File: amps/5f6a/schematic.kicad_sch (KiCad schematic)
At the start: 60 parts, among them T3 2R sec

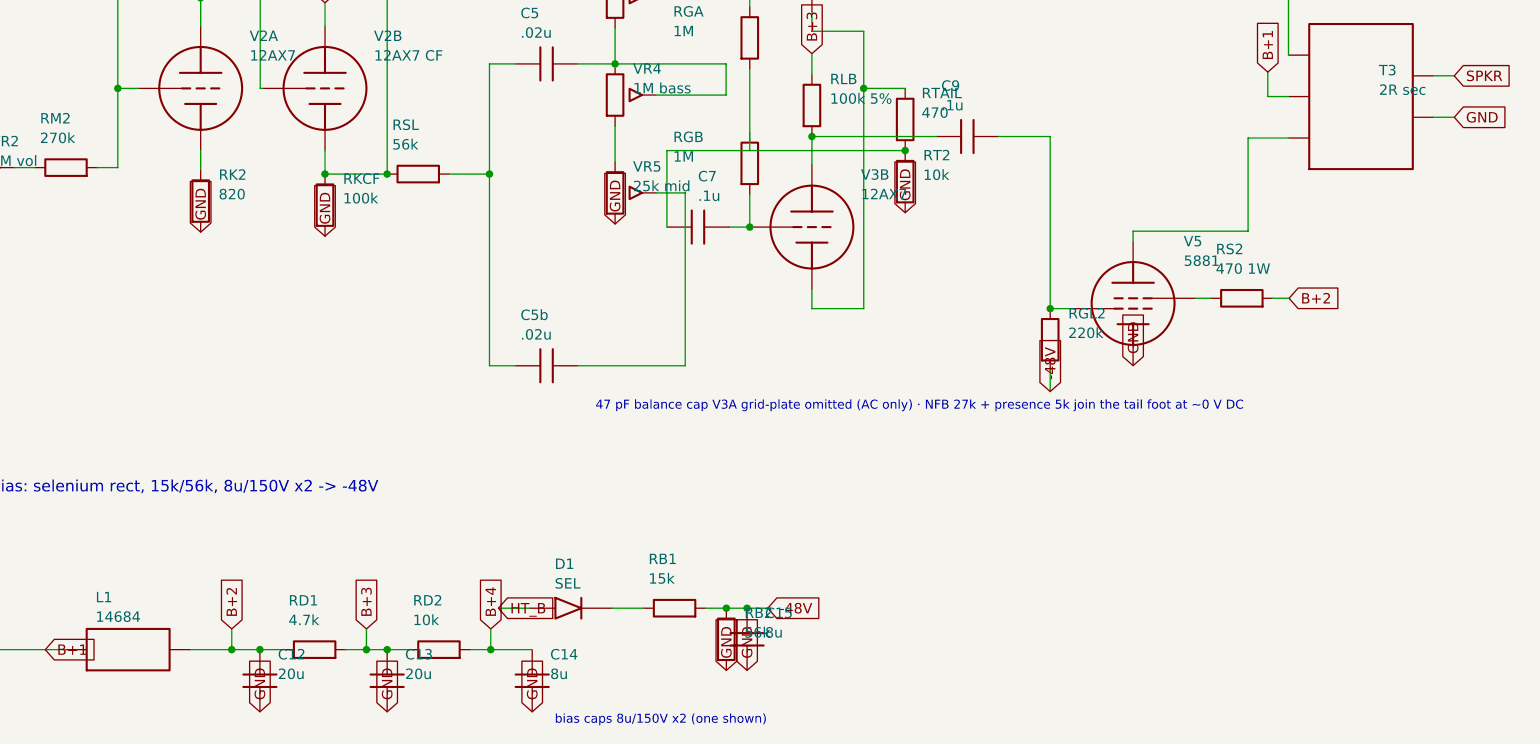
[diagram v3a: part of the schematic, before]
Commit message: Fix: eleven per-amp claims that had drifted from the circuits they describe
Prose that contradicted the corpus it sits in:

* The 5F4 called its ancestor "the 5E-series Super not yet published in this
  archive" while its own meta.yaml derives it from 5E4-A and that circuit has a
  page; the 5F1 said its lineage edge "lands when amps/5e1 exists" while the
  sidebar already links the 5E1. Both now name the documented ancestor. The
  whole corpus was swept for the pattern: 5F2-A's 5F2, 5E5-A's 5E5, 5D3's 5C3,
  5F2-A's and 5F10's earlier revisions and DR103's Sound City are all still
  genuinely absent, so those stay.
* The 5E6-A said its front end gates "within the usual tolerance (worst node
  29.8%)" against a +/-20% convention — a sentence that contradicts itself and
  understates the miss besides. It now states the four nodes that miss, the
  numbers they miss by, and the one dropper-current fault behind all four,
  which is what its own meta.yaml already said. Same defect class as the 5E4-A
  fix in 4c65fa8.
* The 5E5-A's parts list opened "No schematic.kicad_sch is authored in this
  delivery" — one has been authored. Deleted.
* Repo paths were rendering on public pages: four SOURCES entries (5F1, 5E3,
  5F2-A, 5F6, 5F6-A) named amps/<id>/layout.svg, and the 5E5-A, 5E6-A and 5F10
  pages cited voltages.yaml, netlist.cir, verify_amps.py and CONTRIBUTING.md in
  running prose. All reworded as visitor documentation. The 5F10's layout also
  described its own schematic page as "reproduced", which is the one word this
  project must never use about a factory drawing.

Circuit elements that existed only as a caption:

* The 5F6-A's headline change from the 5F6 is the presence control, and it was
  a line of schematic text. It is drawn now — 27k feedback resistor, 5k pot and
  its 0.1 uF wiper cap, at the phase-inverter tail — with designators, parts-list
  rows and chassis-edge placement on both board styles.
* The 5F4's 56k feedback and 5k presence were the same, an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
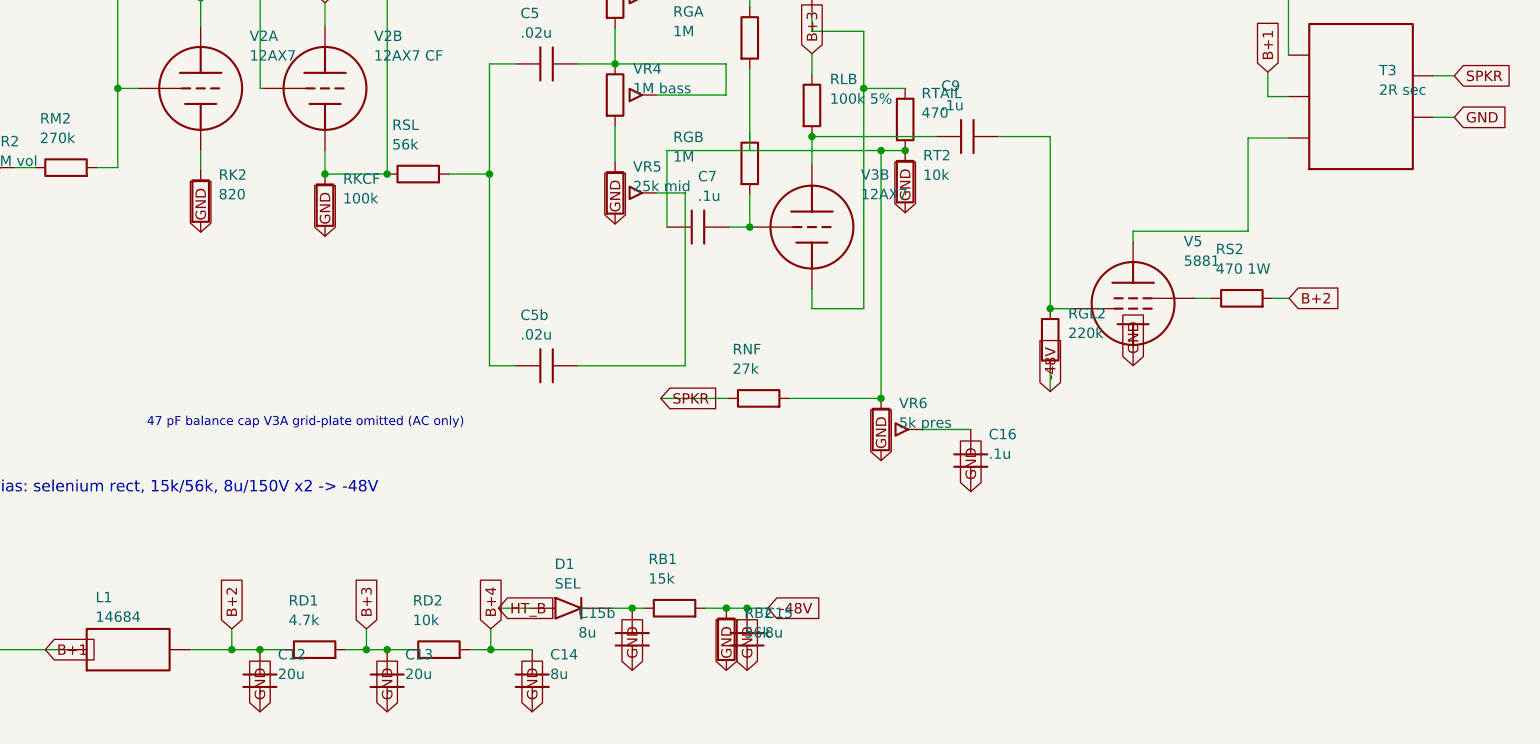
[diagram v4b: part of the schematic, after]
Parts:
- added C15b: 8u, symbol cx:C
- added C16: .1u, symbol cx:C
- added RNF: 27k, symbol cx:R
- added VR6: 5k pres, symbol cx:POT
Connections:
- net GND: now also C15b.2, C16.2, VR6.3
- net SPKR: now also RNF.1
- net at D1.2 (K), RB1.1: now also C15b.1
- net at C7.1, RGA.2, RT2.1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: now also RNF.2, VR6.1
- new net: C16.1, VR6.2 (W)
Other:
- note added: "47 pF balance cap V3A grid-plate omitted (AC only)"
- note removed: "47 pF balance cap V3A grid-plate omitted (AC only) · NFB 27k + presence 5k join the tail foot at ~0 V DC"
- note removed: "bias caps 8u/150V x2 (one shown)"
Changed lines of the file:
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@@
   (wire (pts (xy 158.75 116.62) (xy 168.91 116.62))
     (stroke (width 0) (type default)))
-  (text "47 pF balance cap V3A grid-plate omitted (AC only) · NFB 27k + presence 5k join the tail foot at ~0 V DC" (at 150 148 0)
+  (text "47 pF balance cap V3A grid-plate omitted (AC only)" (at 95 150 0)
     (effects (font (size 1.1 1.1)) (justify left)))
+  (junction (at 185 116.62) (diameter 0) (color 0 0 0 0))
+  (wire (pts (xy 185 116.62) (xy 185 147))
+    (stroke (width 0) (type default)))
+  (junction (at 185 147) (diameter 0) (color 0 0 0 0))
+  (symbol (lib_id "cx:R") (at 170 147 90) (unit 1)
+    (in_bom yes) (on_board yes)
+    (property "Reference" "RNF" (at 166.8 141 270) (effects (font (size 1.27 1.27)) (justify left)))
+    (property "Value" "27k" (at 166.8 143.4 270) (effects (font (size 1.27 1.27)) (justify left))))
+  (wire (pts (xy 173.81 147) (xy 185 147))
+    (stroke (width 0) (type default)))
+  (wire (pts (xy 158 147) (xy 166.19 147))
+    (stroke (width 0) (type default)))
+  (global_label "SPKR" (shape input) (at 158 147 180)
+    (effects (font (size 1.27 1.27)) (justify left)))
+  (symbol (lib_id "cx:POT") (at 185 150.81 0) (unit 1)
+    (in_bom yes) (on_board yes)
+    (property "Reference" "VR6" (at 187.2 147.61 0) (effects (font (size 1.27 1.27)) (justify left)))
+    (property "Value" "5k pres" (at 187.2 150.01 0) (effects (font (size 1.27 1.27)) (justify left))))
+  (global_label "GND" (shape input) (at 185 154.62 270)
+    (effects (font (size 1.27 1.27)) (justify left)))
+  (wire (pts (xy 190.08 150.81) (xy 196 150.81))
+    (stroke (width 0) (type default)))
+  (symbol (lib_id "cx:C") (at 196 154.62 0) (unit 1)
+    (in_bom yes) (on_board yes)
+    (property "Reference" "C16" (at 198.2 151.42 0) (effects (font (size 1.27 1.27)) (justify left)))
+    (property "Value" ".1u" (at 198.2 153.82 0) (effects (font (size 1.27 1.27)) (justify left))))
+  (global_label "GND" (shape input) (at 196 158.43 270)
+    (effects (font (size 1.27 1.27)) (justify left)))
   (wire (pts (xy 176.53 80.9) (xy 194.31 80.9))
     (stroke (width 0) (type default)))
@@
   (wire (pts (xy 152.07 172.72) (xy 155.88 172.72))
     (stroke (width 0) (type default)))
+  (junction (at 154.5 172.72) (diameter 0) (color 0 0 0 0))
+  (symbol (lib_id "cx:C") (at 154.5 176.53 0) (unit 1)
+    (in_bom yes) (on_board yes)
+    (property "Reference" "C15b" (at 147.9 173.33 0) (effects (font (size 1.27 1.27)) (justify left)))
+    (property "Value" "8u" (at 147.9 175.73 0) (effects (font (size 1.27 1.27)) (justify left))))
+  (global_label "GND" (shape input) (at 154.5 180.34 270)
+    (effects (font (size 1.27 1.27)) (justify left)))
   (symbol (lib_id "cx:R") (at 159.69 172.72 90) (unit 1)
     (in_bom yes) (on_board yes)
@@
   (global_label "-48V" (shape input) (at 171.12 172.72 0)
     (effects (font (size 1.27 1.27)) (justify left)))
-  (text "bias caps 8u/150V x2 (one shown)" (at 145 186.5 0)
-    (effects (font (size 1.1 1.1)) (justify left)))
   (sheet_instances (path "/" (page "1")))
 )

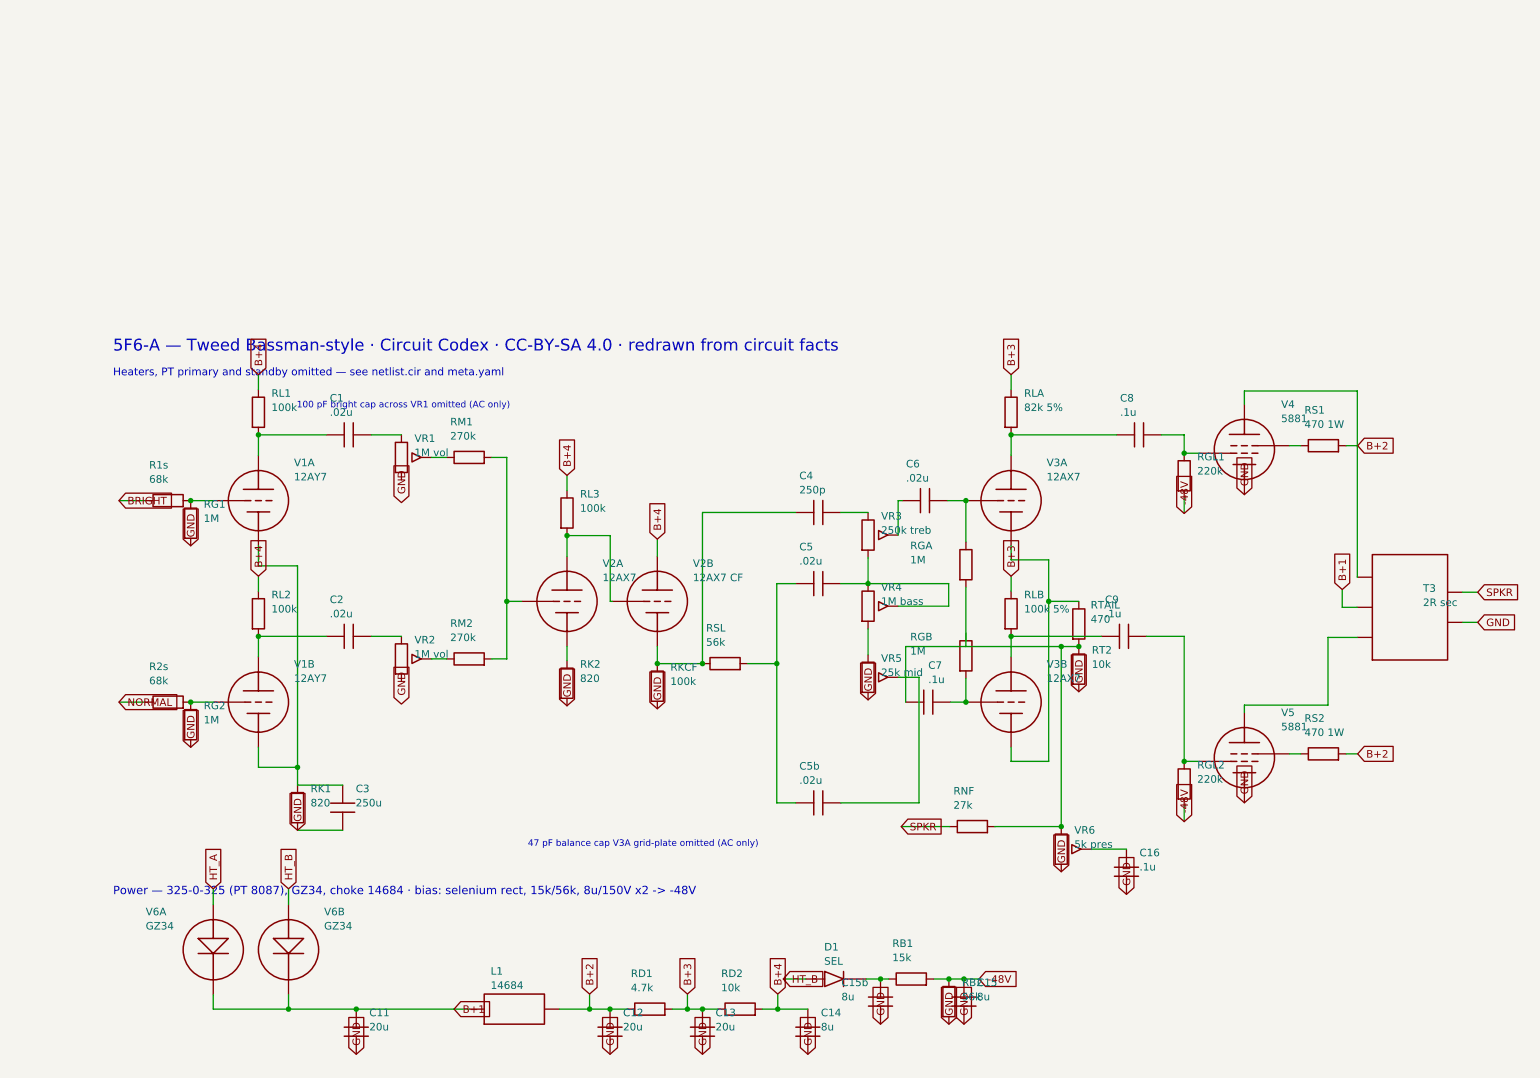
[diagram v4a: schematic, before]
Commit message: Update: regenerate every drawing the four merged units changed
The four parallel units all rewrote generators, so their committed artifacts
were each generated against only their own third of the merged pipeline. Every
schematic, both layout styles, the social cards and the manifest are rebuilt
here from the merged sources, so what ships is what the merged generators draw.

One integration fault the rebuild exposed, invisible to any single unit:

- 5E5-A: the note explaining that the Presence wiper and the 100k feedback
  resistor land on V3A's GRID (not its cathode, as on the 5F4) was added as a
  hand-placed `s.text()` at a coordinate chosen before the sheet gained a
  reserved notes band. Merged, it printed through the -32V bias label. Moved to
  `note()`, which wraps prose into that band — the exact failure mode the band
  was built to end.

Three conflicts resolved against docs/lettering-conventions.md rather than by
picking a side, since two units had corrected the same lines for different
reasons:

- 5E5-A tone/feedback caps take the corrected designators (C7, C8, C9, RNF —
  `C_tr1`/`C_NFB` were generator identifiers that had leaked onto a published
  board) with the house-derived lettering (`.01u 400V`, `500p`, `.1u 200V`).
  Dropping the working voltage or writing `.0005u` would have lost a rating the
  source prints and re-broken the pF/µF decade rule.
- 5D3 C6 and 6G6-B's three cathode resistors take the SI-prefix form the
  convention binds (`.005u`, `2.7k`, `1.5k`), keeping the ground-flag direction
  fix and the removal of the second `gnd()` that shorted each cathode it biased.
- 5F6-A's bias supply keeps both 8 µF cans drawn — the second was previously a
  parenthetical claiming one of two was shown — at the coordinates that clear
  the title-block strip.

All gates green, including check_value_consistency at zero disagreements.

🤖 Generated with [Claude Code](https://claude.com/claude-code)

Co-Authored-By: Claude Fable 5 <noreply@anthropic.com>
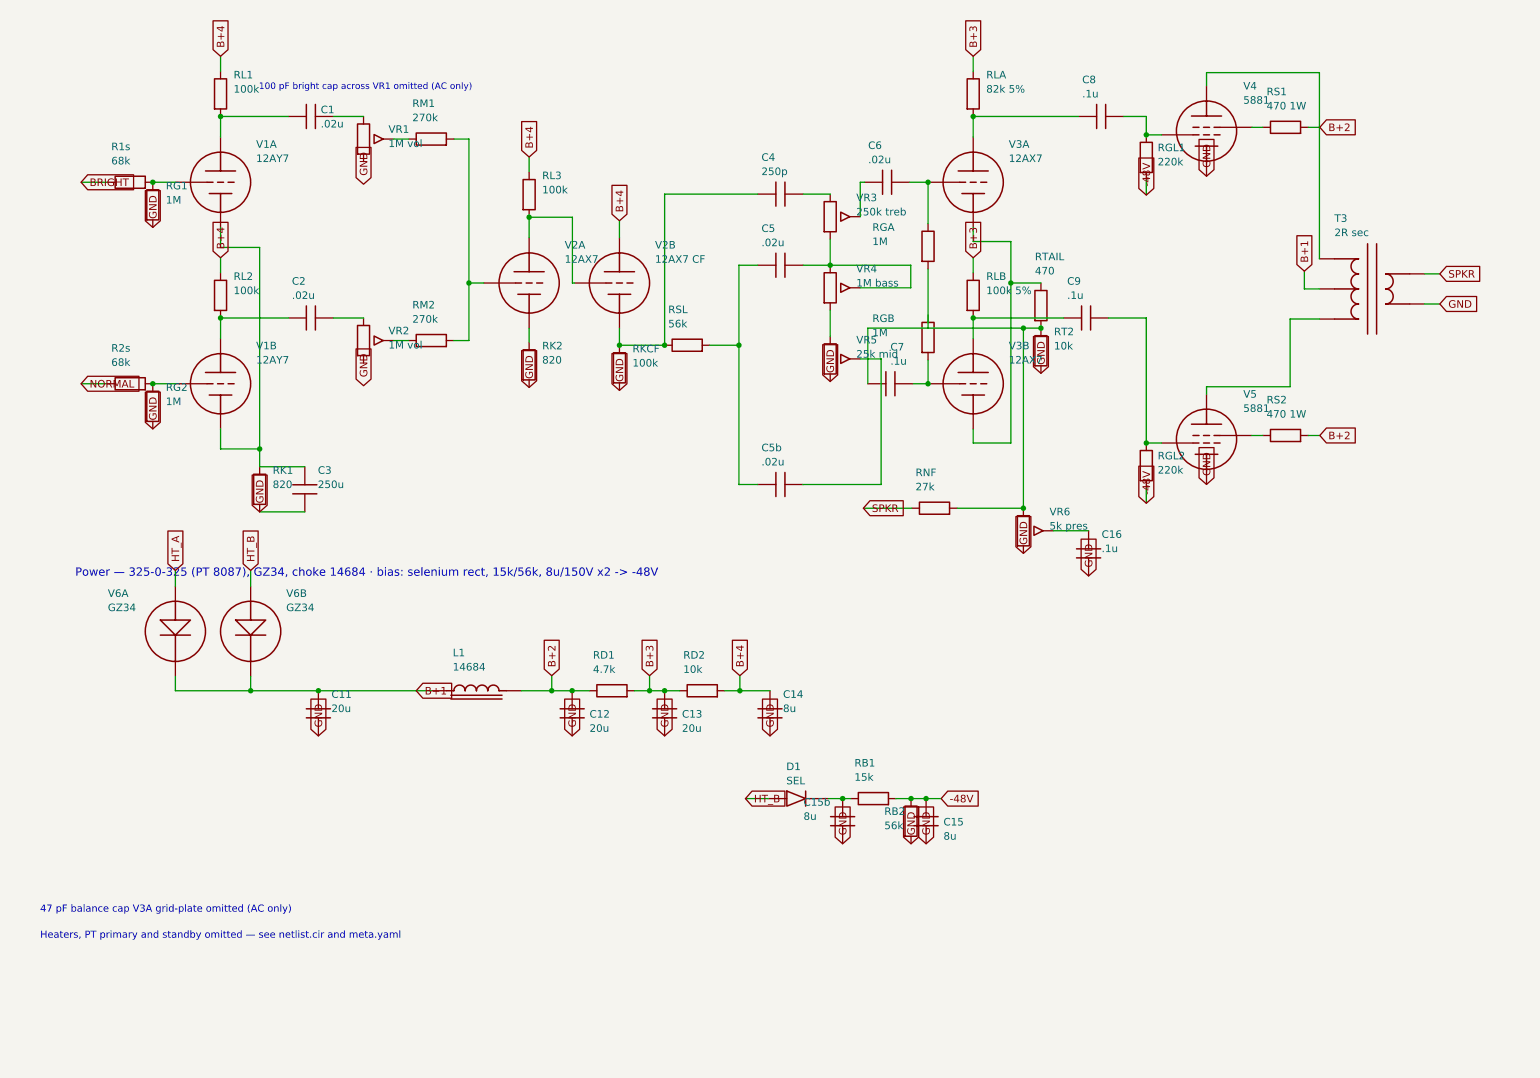
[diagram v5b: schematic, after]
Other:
- note removed: "5F6-A — Tweed Bassman-style · Circuit Codex · CC-BY-SA 4.0 · redrawn from circuit facts"
- company: (none) -> Circuit Codex
- title: (none) -> 5F6-A — Tweed Bassman-style

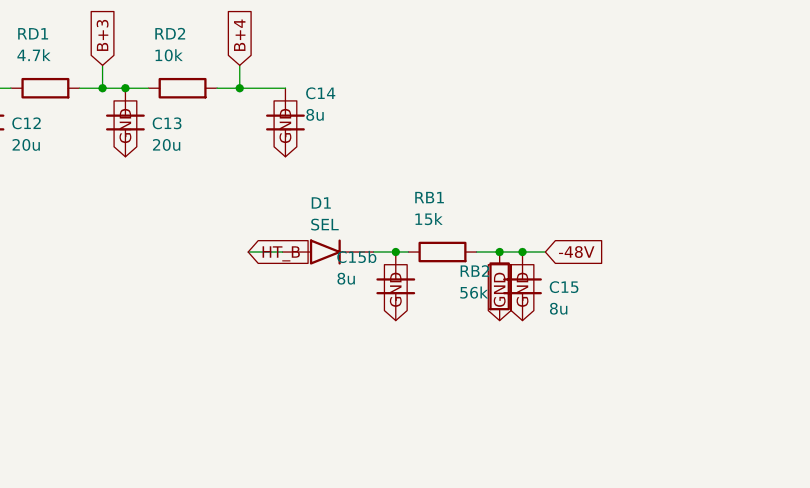
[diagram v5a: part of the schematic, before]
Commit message: Fix: 5F6-A bias reservoir's designator printed through the rectifier
The second bias can is newly drawn rather than named in a parenthetical, and it
inherited a hand-placed label offset from the layout it was authored against.
Merged, that offset put "C15b" on D1's cathode bar: the designator read as if it
belonged to the rectifier, and the bar struck through the C.

The sheet gate did not catch it. Its clash test compares label boxes against
symbol BODY boxes, and the cathode bar sits far enough out that the overlap
stayed under the 0.5 mm threshold — visible to a reader, invisible to the
metric. This is exactly why AGENTS.md requires eyes on every changed figure
rather than a green gate, and it was found by looking at the render.

Dropping the authored offset lets place_labels() choose, which puts the block
clear to the right of its own plates. No library or threshold was touched: one
sheet had a bad anchor, so one anchor is gone. Re-checked by eye — the bias
supply now reads HT_B -> D1 -> C15b reservoir -> RB1 15k -> -48V with RB2
bleeder and C15 filter, which is what the parts list says each of them does.

🤖 Generated with [Claude Code](https://claude.com/claude-code)

Co-Authored-By: Claude Fable 5 <noreply@anthropic.com>
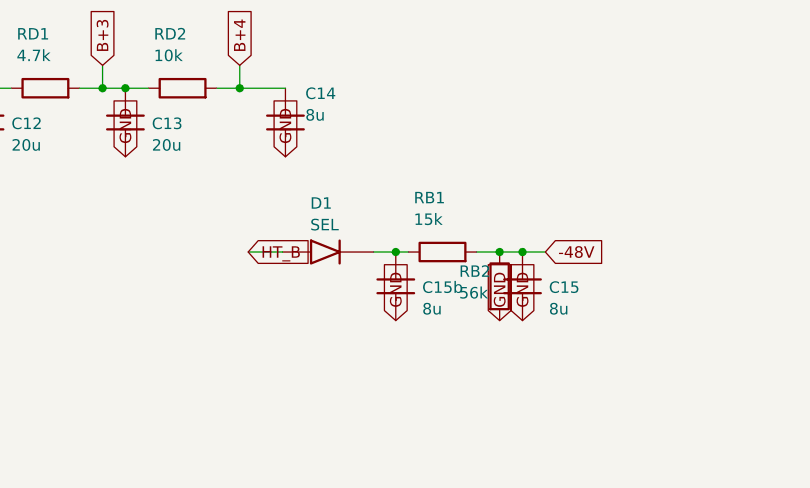
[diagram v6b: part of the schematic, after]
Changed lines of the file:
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@@
   (symbol (lib_id "cx:C") (at 148.109 146.088 0) (unit 1)
     (in_bom yes) (on_board yes)
-    (property "Reference" "C15b" (at 141.509 142.888 0) (effects (font (size 1.27 1.27)) (justify left)))
-    (property "Value" "8u" (at 141.509 145.288 0) (effects (font (size 1.27 1.27)) (justify left))))
+    (property "Reference" "C15b" (at 151.041 146.226 0) (effects (font (size 1.27 1.27)) (justify left)))
+    (property "Value" "8u" (at 151.041 148.626 0) (effects (font (size 1.27 1.27)) (justify left))))
   (global_label "GND" (shape input) (at 148.109 149.898 270)
     (effects (font (size 1.27 1.27)) (justify left)))
